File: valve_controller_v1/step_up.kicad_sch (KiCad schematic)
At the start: 17 parts, among them SW4 Voltage Selector, U5 LT218, U6 LMR62421XMF

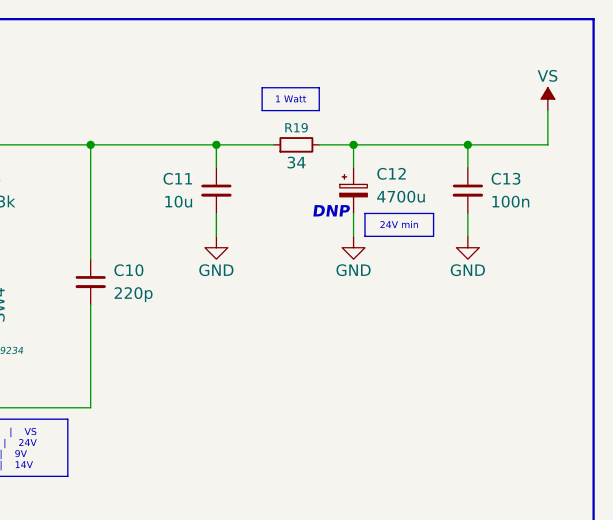
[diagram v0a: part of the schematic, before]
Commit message: Routed PCB and added 3D models
Routed the entire PCB
Added 3D Models for the RAK module and Battery Holder
Improved Silkscreen
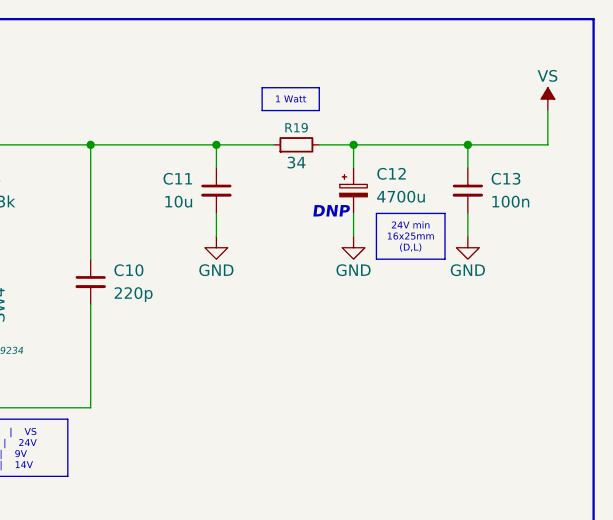
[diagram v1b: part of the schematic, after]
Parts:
- C12: footprint Capacitor_THT:CP_Radial_D18.0mm_P7.50mm -> Capacitor_THT:CP_Radial_D16.0mm_P7.50mm
- SW4: footprint Package_SO:SO-4_4.4x4.3mm_P2.54mm -> Button_Switch_SMD:SW_DIP_SPSTx02_Slide_Omron_A6H-2101_W6.15mm_P1.27mm
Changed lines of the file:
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@@
 		)
 	)
-	(text_box "24V min"
-		(exclude_from_sim no)
-		(at 167.64 36.83 0)
-		(size 7.62 2.54)
+	(text_box "24V min\n16x25mm (D,L)"
+		(exclude_from_sim no)
+		(at 168.91 36.83 0)
+		(size 7.62 5.08)
 		(margins 0.9525 0.9525 0.9525 0.9525)
 		(stroke
@@
 			)
 		)
-		(property "Footprint" "Package_SO:SO-4_4.4x4.3mm_P2.54mm"
+		(property "Footprint" "Button_Switch_SMD:SW_DIP_SPSTx02_Slide_Omron_A6H-2101_W6.15mm_P1.27mm"
 			(at 123.19 46.99 0)
 			(effects
@@
 			)
 		)
-		(property "Footprint" "Capacitor_THT:CP_Radial_D18.0mm_P7.50mm"
+		(property "Footprint" "Capacitor_THT:CP_Radial_D16.0mm_P7.50mm"
 			(at 166.37 34.29 0)
 			(effects

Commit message: Final corrections for manufacturing
Created new condenser footprint to better represent the actual position
Created new voltage selector ip switch footprint
Selected bigger footprint for R19 (was 1206 now is 2512 as in the legacy version)
Corrected D5 footprint (was SOD-123 now is SMA)
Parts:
- C12: footprint Capacitor_THT:CP_Radial_D16.0mm_P7.50mm -> Wisflow:CP_Horizontal_D16_L25_P7.5mm
- D5: footprint Diode_SMD:D_SC-80 -> Diode_SMD:D_SMA
- R19: footprint Resistor_SMD:R_1206_3216Metric -> Resistor_SMD:R_2512_6332Metric
- SW4: footprint Button_Switch_SMD:SW_DIP_SPSTx02_Slide_Omron_A6H-2101_W6.15mm_P1.27mm -> Wisflow:SMXMS-02
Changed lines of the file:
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@@
 			)
 		)
-		(property "Footprint" "Resistor_SMD:R_1206_3216Metric"
+		(property "Footprint" "Resistor_SMD:R_2512_6332Metric"
 			(at 160.02 29.21 0)
 			(effects
@@
 			)
 		)
-		(property "Footprint" "Button_Switch_SMD:SW_DIP_SPSTx02_Slide_Omron_A6H-2101_W6.15mm_P1.27mm"
+		(property "Footprint" "Wisflow:SMXMS-02"
 			(at 123.19 46.99 0)
 			(effects
@@
 			)
 		)
-		(property "Footprint" "Capacitor_THT:CP_Radial_D16.0mm_P7.50mm"
+		(property "Footprint" "Wisflow:CP_Horizontal_D16_L25_P7.5mm"
 			(at 166.37 34.29 0)
 			(effects
@@
 			)
 		)
-		(property "Footprint" "Diode_SMD:D_SC-80"
+		(property "Footprint" "Diode_SMD:D_SMA"
 			(at 96.52 41.91 90)
 			(effects
